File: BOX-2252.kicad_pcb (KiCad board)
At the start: 2 copper layers, 50.5 x 70 mm, 65 parts, among them P1 MYSX_1.5, P2 CONN_02X03, P3 CONN_01X03, P4 CONN_01X03, Q1 DMP3056L-7, Q2 DMP3056L-7, U1 LD1117DT33TR, U2 TPS61097A, U3 ATSHA204A, U4 RFM69HW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

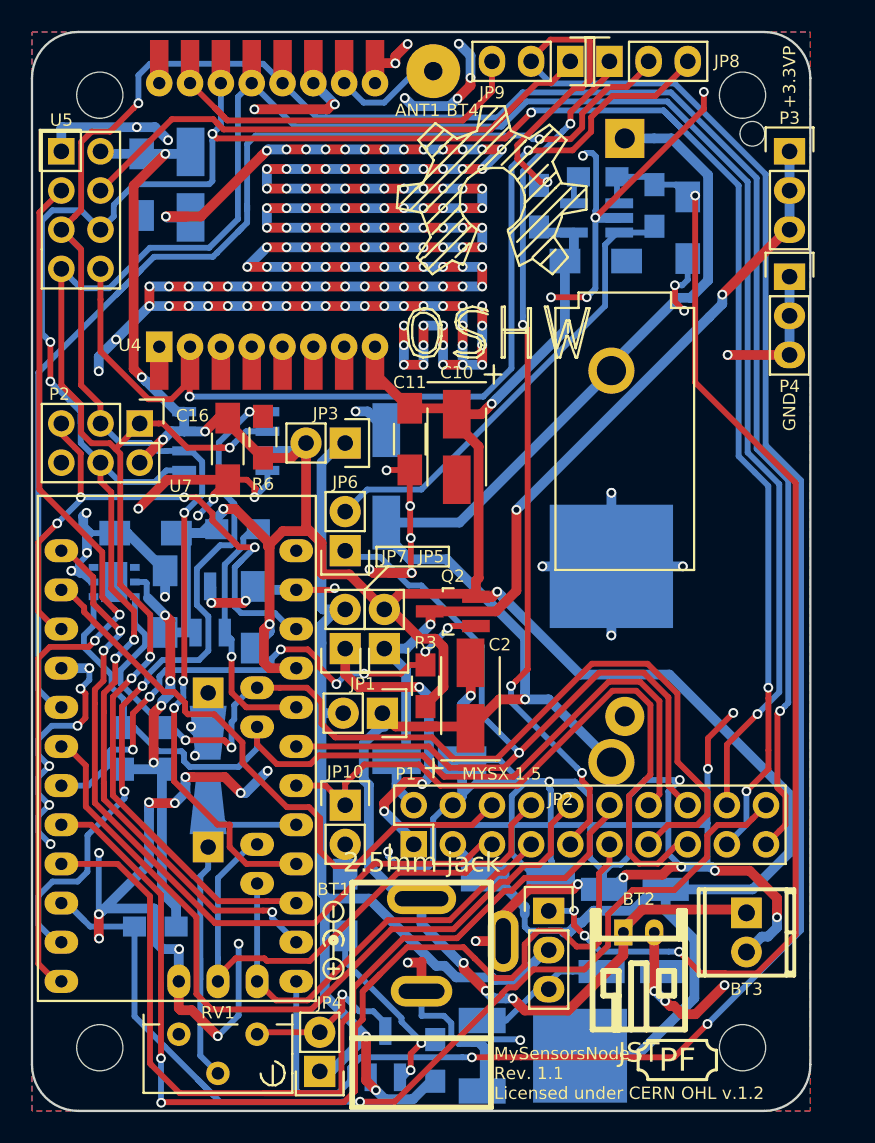
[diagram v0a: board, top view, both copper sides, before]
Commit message: Minor beautifications and updated CHANGES.txt
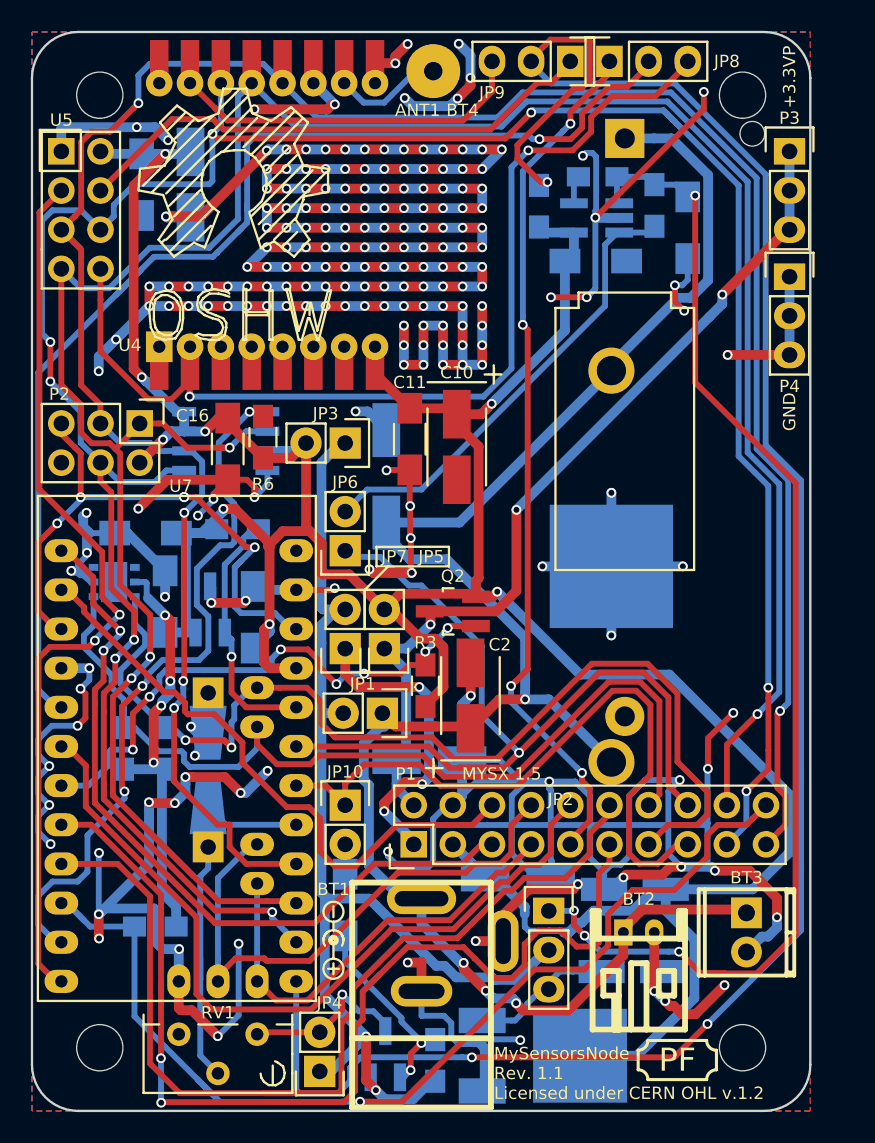
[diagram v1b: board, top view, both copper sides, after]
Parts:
- moved OSHW_LOGO 16.8 mm to (134.5, 41.0)
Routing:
- net RESET: track 38.3 -> 38.0 mm, vias 4 -> 5

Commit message: Updated U1 footprint
U1 footprint is now available in the mysensors-kicad repository
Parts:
- U1: footprint SMD_Packages:DPAK-2 -> mysensors_obscurities:d-pak-kcswalter
- moved U1 5.14 mm to (155.7, 117.0)
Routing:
- net GND: track 553.1 -> 546.3 mm
- net Net-(C4-Pad1): track 9.94 -> 7.89 mm
- net Net-(BT1-Pad3): track 119.5 -> 120.6 mm
- net +3V3: track 257.3 -> 256.4 mm
